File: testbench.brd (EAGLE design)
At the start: 100 x 100 mm, 47 parts, among them T1 C8492, T2 C8492, T3 C8545, T4 C8545, X1 MKDSN1,5/2-5,08

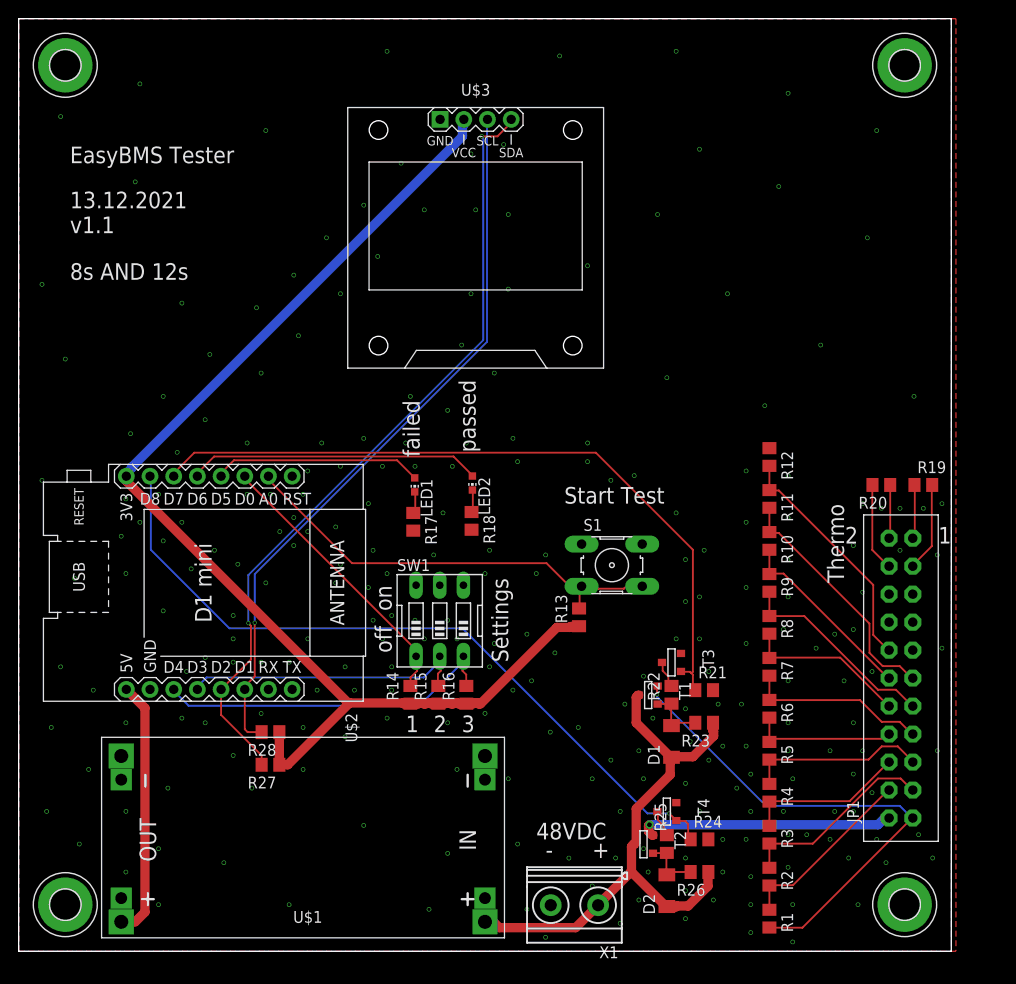
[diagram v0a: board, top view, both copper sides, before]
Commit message: fixed PFETs reverse orientation, v1.2
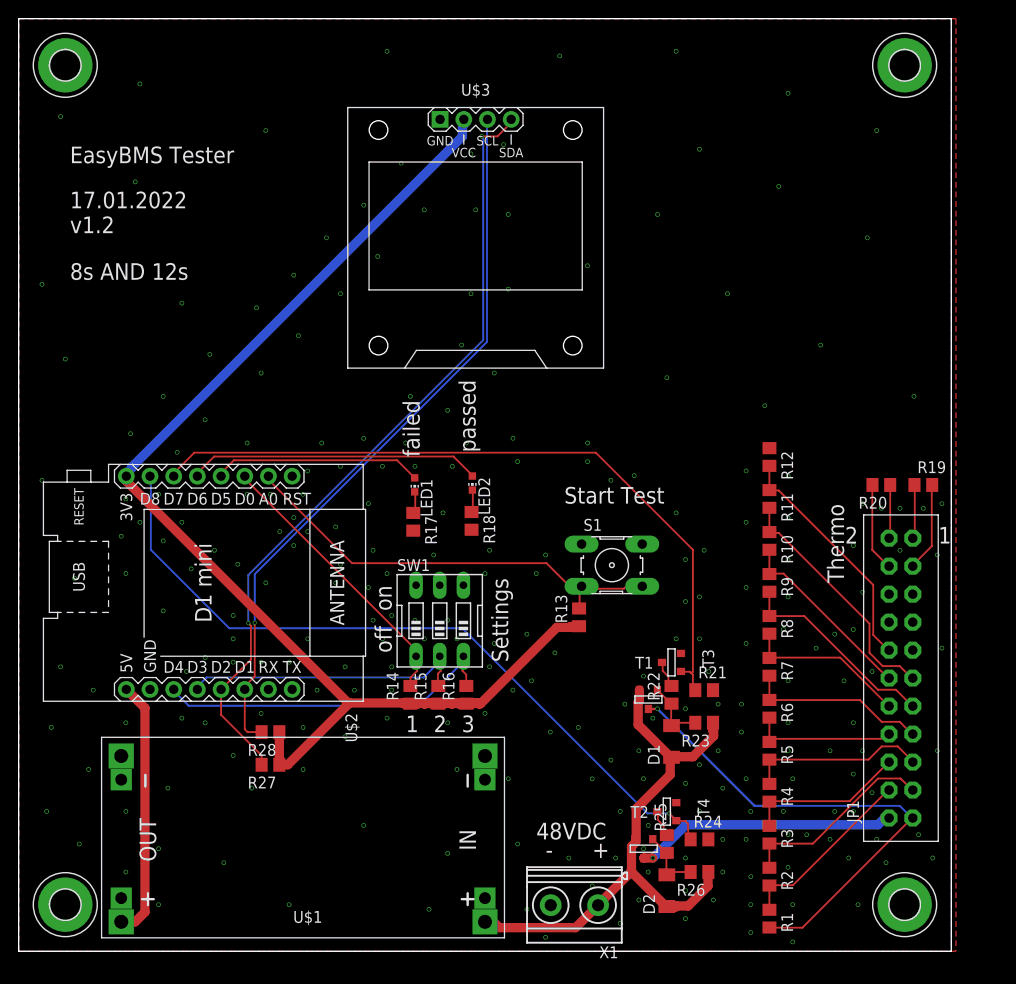
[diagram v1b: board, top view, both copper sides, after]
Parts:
- moved T1 0.50 mm to (67.5, 27.0), turned to 0 degrees
- moved T2 0.50 mm to (67.0, 11.0), turned to 0 degrees
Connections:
- net 48VDC: now also T1.2, T2.2; no longer T1.1, T2.1
- net BATSIM: now also T1.1; no longer T1.2
- net N$19: now also T2.1; no longer T2.2
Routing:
- net BATSIM: track 54.2 -> 53.4 mm
- net N$19: track 27.4 -> 28.1 mm
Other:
- board text added: "17.01.2022 v1.2"
- board text removed: "13.12.2021 v1.1"

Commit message: new smd footprint of BMS connector integrated
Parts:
- JP1: device pinhead_own:2X11_MEB12S_MODULSEITE -> pinhead_own:2X11_MEB12S_MODULSEITE_SMD
- moved R20 24.8 mm to (82.0, 72.5)
- moved R19 24.2 mm to (88.0, 72.5)
- moved R1 24.0 mm to (75.5, 27.0)
- moved R10 24.0 mm to (75.5, 67.5)
- moved R11 24.0 mm to (75.5, 72.0)
- moved R12 24.0 mm to (75.5, 76.5)
- moved R2 24.0 mm to (75.5, 31.5)
- moved R3 24.0 mm to (75.5, 36.0)
- moved R4 24.0 mm to (75.5, 40.5)
- moved R5 24.0 mm to (75.5, 45.0)
- moved R6 24.0 mm to (75.5, 49.5)
- moved R7 24.0 mm to (75.5, 54.0)
- moved R8 24.0 mm to (75.5, 58.5)
- moved R9 24.0 mm to (75.5, 63.0)
- moved JP1 21.5 mm to (87.9, 49.7), turned to 270 degrees
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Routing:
- net N$11: track 25.7 -> 50.5 mm
- net BATSIM: track 53.4 -> 33.5 mm, vias 1 -> 2
- net D7: track 77.7 -> 67.6 mm
- net D8: track 79.5 -> 70.0 mm
- net 48VDC: track 60.1 -> 67.5 mm
- net N$1: track 19.7 -> 13.0 mm
- net N$3: track 17.2 -> 10.5 mm
- net N$5: track 16.0 -> 11.3 mm
- net A0: track 48.0 -> 43.5 mm
- net N$2: track 21.4 -> 17.0 mm
- net +3V3: track 129.9 -> 133.9 mm
- net N$4: track 19.3 -> 15.7 mm
- net N$7: track 17.6 -> 14.1 mm
- net THERMO1IN: track 5.89 -> 8.14 mm
- net N$10: track 26.3 -> 28.5 mm
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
